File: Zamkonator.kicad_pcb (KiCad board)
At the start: 2 copper layers, 75 x 75 mm, 127 parts, among them J1 Screw_Terminal_01x06, J2 RJ45_Abracon_ARJP11A-MASA-B-A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, J3 Conn_01x08_Male, J4 Conn_02x06_Counter_Clockwise, J5 Conn_01x04_Female, J6 Conn_01x03_Female, K1 SRD-DC3V-SL-C, Q1 BCP56, T1 HR051142, U1 RTL8201F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

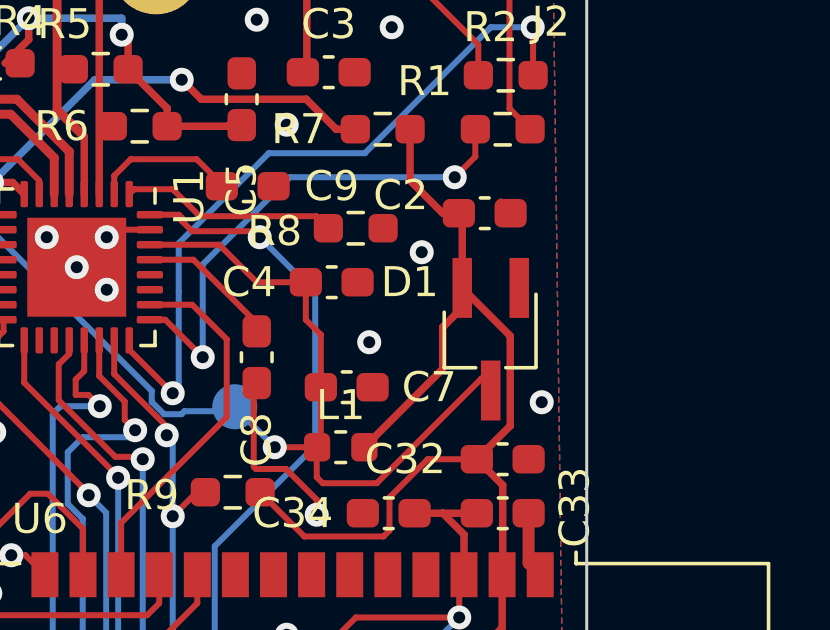
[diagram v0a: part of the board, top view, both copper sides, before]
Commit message: Fixup diode footprint and add more LCSC numbers
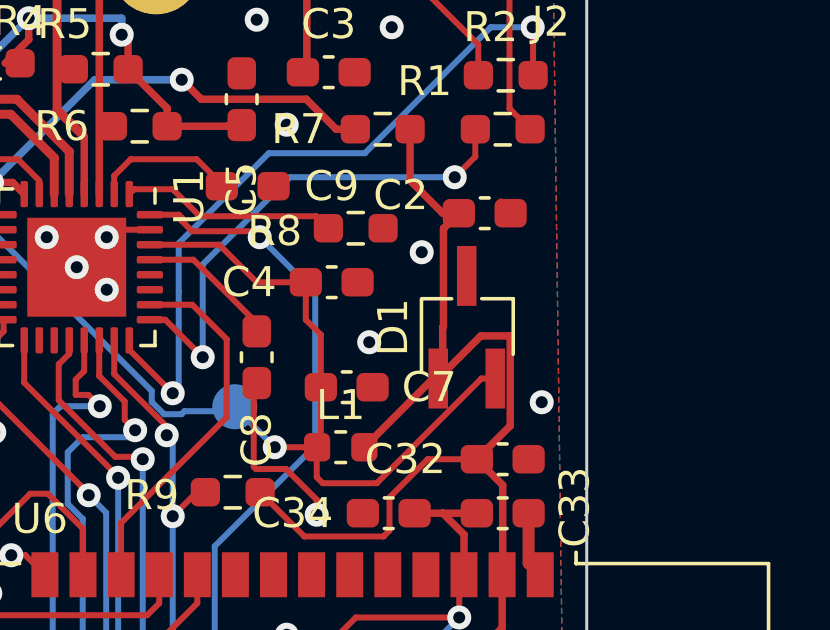
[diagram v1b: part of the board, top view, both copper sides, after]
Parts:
- C10: value 0.1u -> 100n
- moved D1 0.89 mm to (71.0, 40.0), turned to 90 degrees
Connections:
- D1 pad 1: GND -> +3.3V
- D1 pad 2: +3.3V -> Net-(C4-Pad1)
- D1 pad 3: Net-(C4-Pad1) -> GND
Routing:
- net +3.3V: track 265.6 -> 266.4 mm

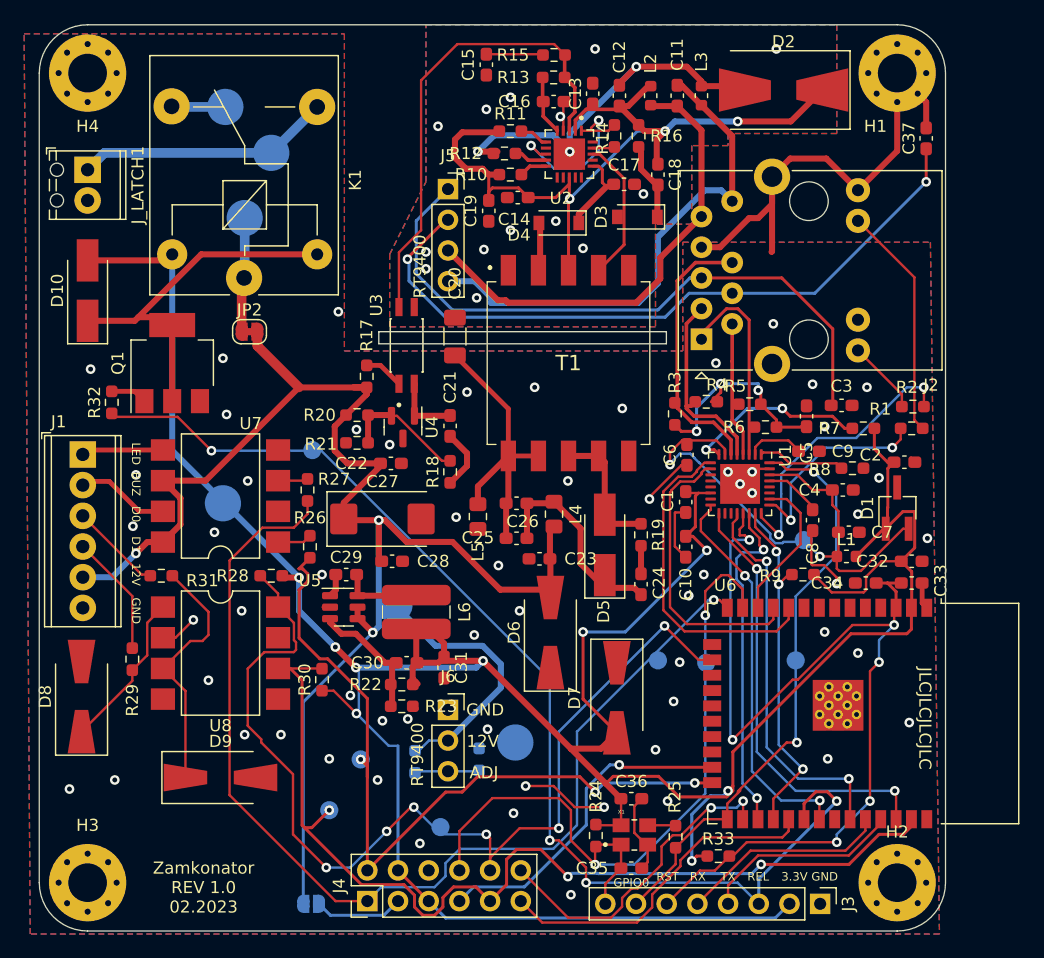
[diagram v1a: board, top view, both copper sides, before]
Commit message: Add more LCSC markings, change to electrolytic caps :
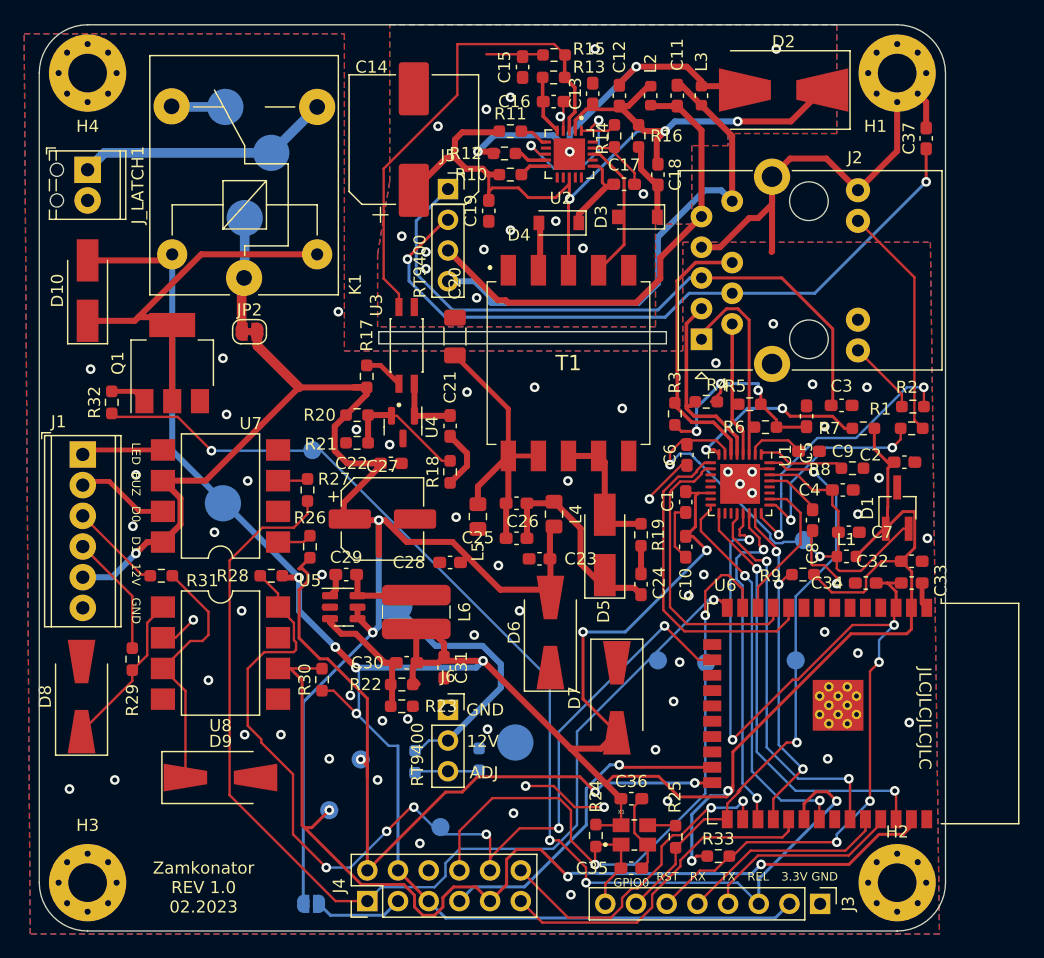
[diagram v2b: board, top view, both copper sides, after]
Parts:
- C12, C13: value 0.1u 100V -> 100n 100V
- C14: footprint Capacitor_SMD:C_0603_1608Metric_Pad1.08x0.95mm_HandSolder -> Capacitor_SMD:CP_Elec_10x10.5
- C27: footprint Capacitor_Tantalum_SMD:CP_EIA-7343-30_AVX-N_Pad2.25x2.55mm_HandSolder -> Capacitor_SMD:CP_Elec_6.3x7.7
- D1: value S2303 -> SM03
- R28, R30: value 140 -> 10k
- moved C14 9.85 mm to (31.0, 9.50), turned to 90 degrees
- moved C28 4.80 mm to (34.0, 44.5), turned to 180 degrees
- moved C15 3.01 mm to (40.0, 3.50)
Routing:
- net Net-(C4-Pad1): track 45.1 -> 0.00 mm, vias 2 -> 0
- net +3.3V: track 266.4 -> 311.4 mm, vias 9 -> 11
- net Net-(C12-Pad1): track 69.0 -> 73.6 mm
- net VSS: track 4.53 -> 8.31 mm, vias 14 -> 15
- net Net-(R13-Pad2): track 39.9 -> 40.9 mm

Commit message: Switch to LCSC RJ45 socket
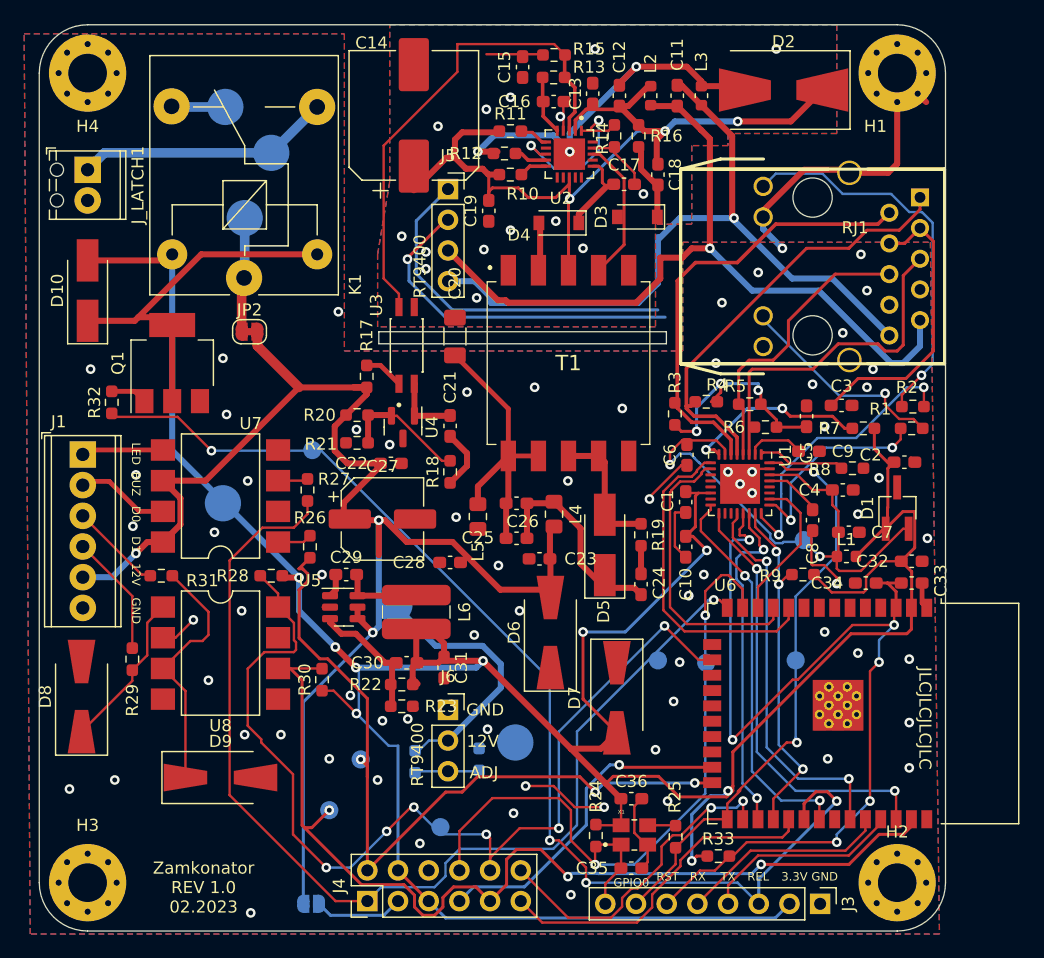
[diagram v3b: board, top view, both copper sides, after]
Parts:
- removed C37: 100n, Capacitor_SMD:C_0603_1608Metric_Pad1.08x0.95mm_HandSolder
- removed J2: RJ45_Abracon_ARJP11A-MASA-B-A-EMU2, Connector_RJ:RJ45_Abracon_ARJP11A-MA_Horizontal
- added RJ1: HY931147C, project specific:RJ45-TH_HY931147C, F.Cu at (66.4, 20.0)
- moved C14 2.00 mm to (31.0, 7.50)
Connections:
- C3 pad 1: /RT9400_VA1 -> Net-(C3-Pad1)
- J5 pad 1: /RT9400_VA1 -> unconnected-(J5-Pad1)
- J5 pad 2: /RT9400_VA2 -> unconnected-(J5-Pad2)
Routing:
- net /RT9400_VA2: track 58.0 -> 0.00 mm, vias 2 -> 0
- net /RT9400_VA1: track 53.0 -> 0.00 mm
- net unconnected-(J5-Pad1): track 0.00 -> 29.3 mm
- net unconnected-(J5-Pad2): track 0.00 -> 29.2 mm, vias 0 -> 1
- net /RT9400_VB1: track 38.9 -> 65.6 mm, vias 0 -> 1
- net Net-(R2-Pad1): track 6.15 -> 32.4 mm, vias 0 -> 1
- net Net-(C3-Pad1): track 0.00 -> 24.0 mm
- net Net-(R4-Pad1): track 16.3 -> 36.6 mm
- net /RT9400_VB2: track 42.7 -> 60.1 mm, vias 0 -> 1
- net Net-(R3-Pad1): track 22.4 -> 37.2 mm
- net GND: track 85.2 -> 71.5 mm, vias 61 -> 70
- net Net-(R5-Pad1): track 12.0 -> 24.0 mm
- net Net-(R6-Pad1): track 16.8 -> 28.7 mm
- net Net-(R1-Pad1): track 19.4 -> 18.0 mm, vias 0 -> 1

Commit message: Silkscreen fixes
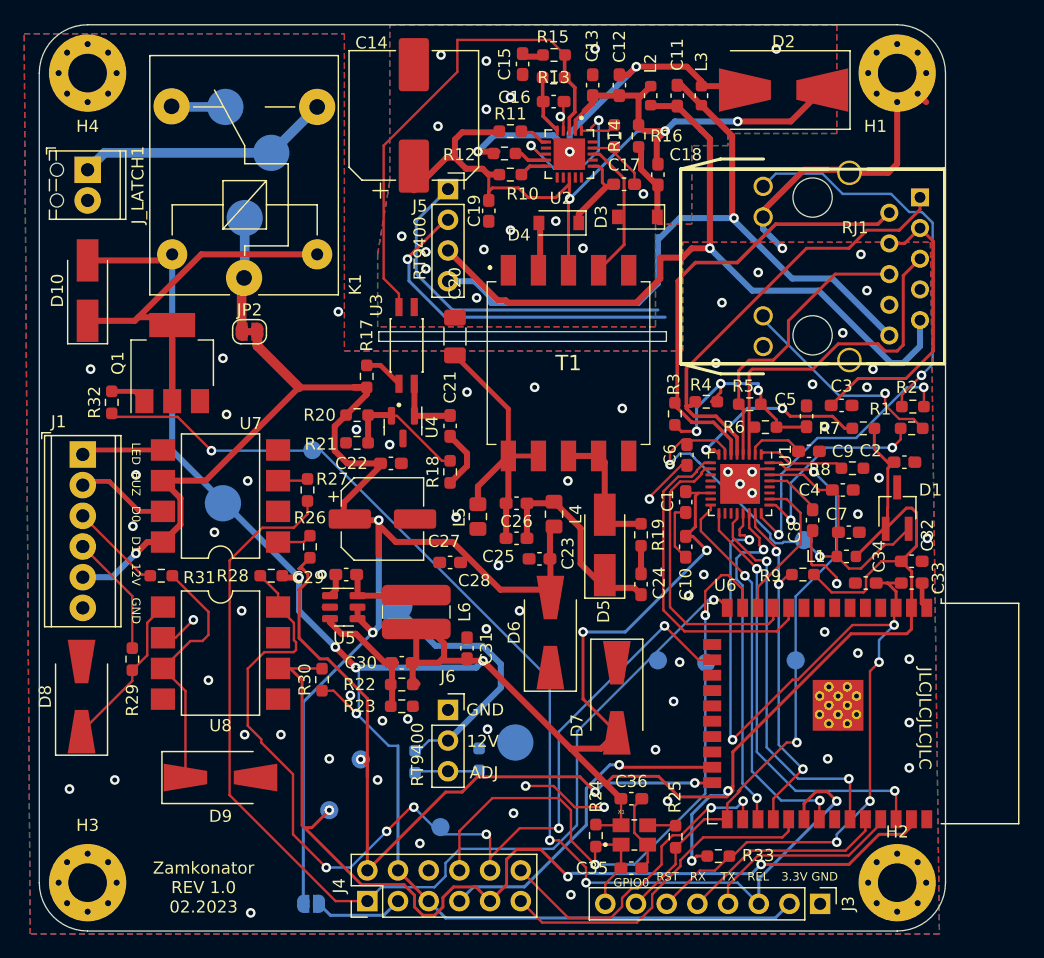
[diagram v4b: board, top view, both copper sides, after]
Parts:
- moved C31 2.48 mm to (35.4, 51.6), turned to 90 degrees
- moved C12 0.87 mm to (48.0, 5.00)
- moved C13 0.70 mm to (45.8, 5.00)
- moved C30 0.40 mm to (30.0, 52.8)
- moved C15 0.25 mm to (40.0, 3.25)
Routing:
- net +3.3V: track 311.4 -> 266.8 mm, vias 11 -> 9
- net Net-(C4-Pad1): track 0.00 -> 44.0 mm, vias 0 -> 2
- net Net-(C15-Pad1): track 4.71 -> 1.83 mm
- net VSS: vias 15 -> 17
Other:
- outline, holes or cut-outs redrawn
